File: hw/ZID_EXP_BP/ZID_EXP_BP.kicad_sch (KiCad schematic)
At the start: 41 parts, among them J1 FROM ZID, J2 Conn_02x05_2.54mm, J3 Conn_02x05_2.54mm, J4 USB-C PWR ONLY, J6 Conn_02x03_Odd_Even, J7 Conn_02x03_Odd_Even, J9 HDR 2x10 Pin, Q1 DMG2305UX, U1 74HCT138

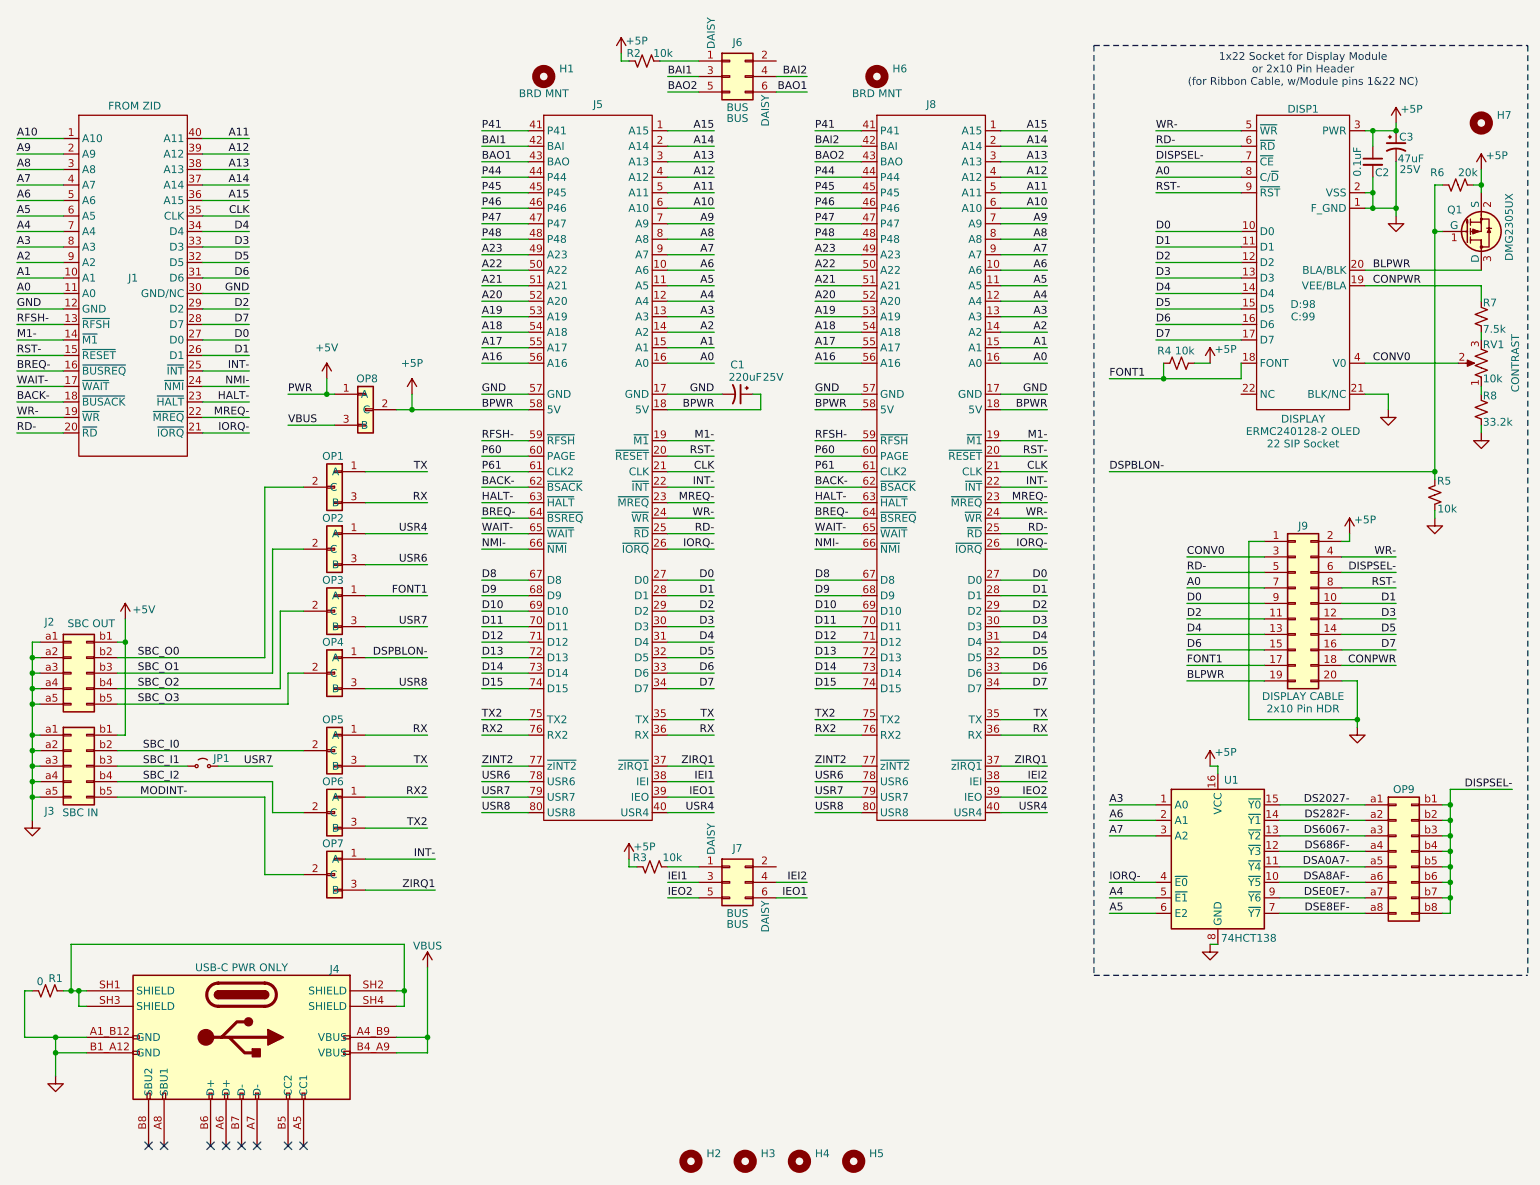
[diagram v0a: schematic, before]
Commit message: EXP-BP: Bypass caps, contrast R values
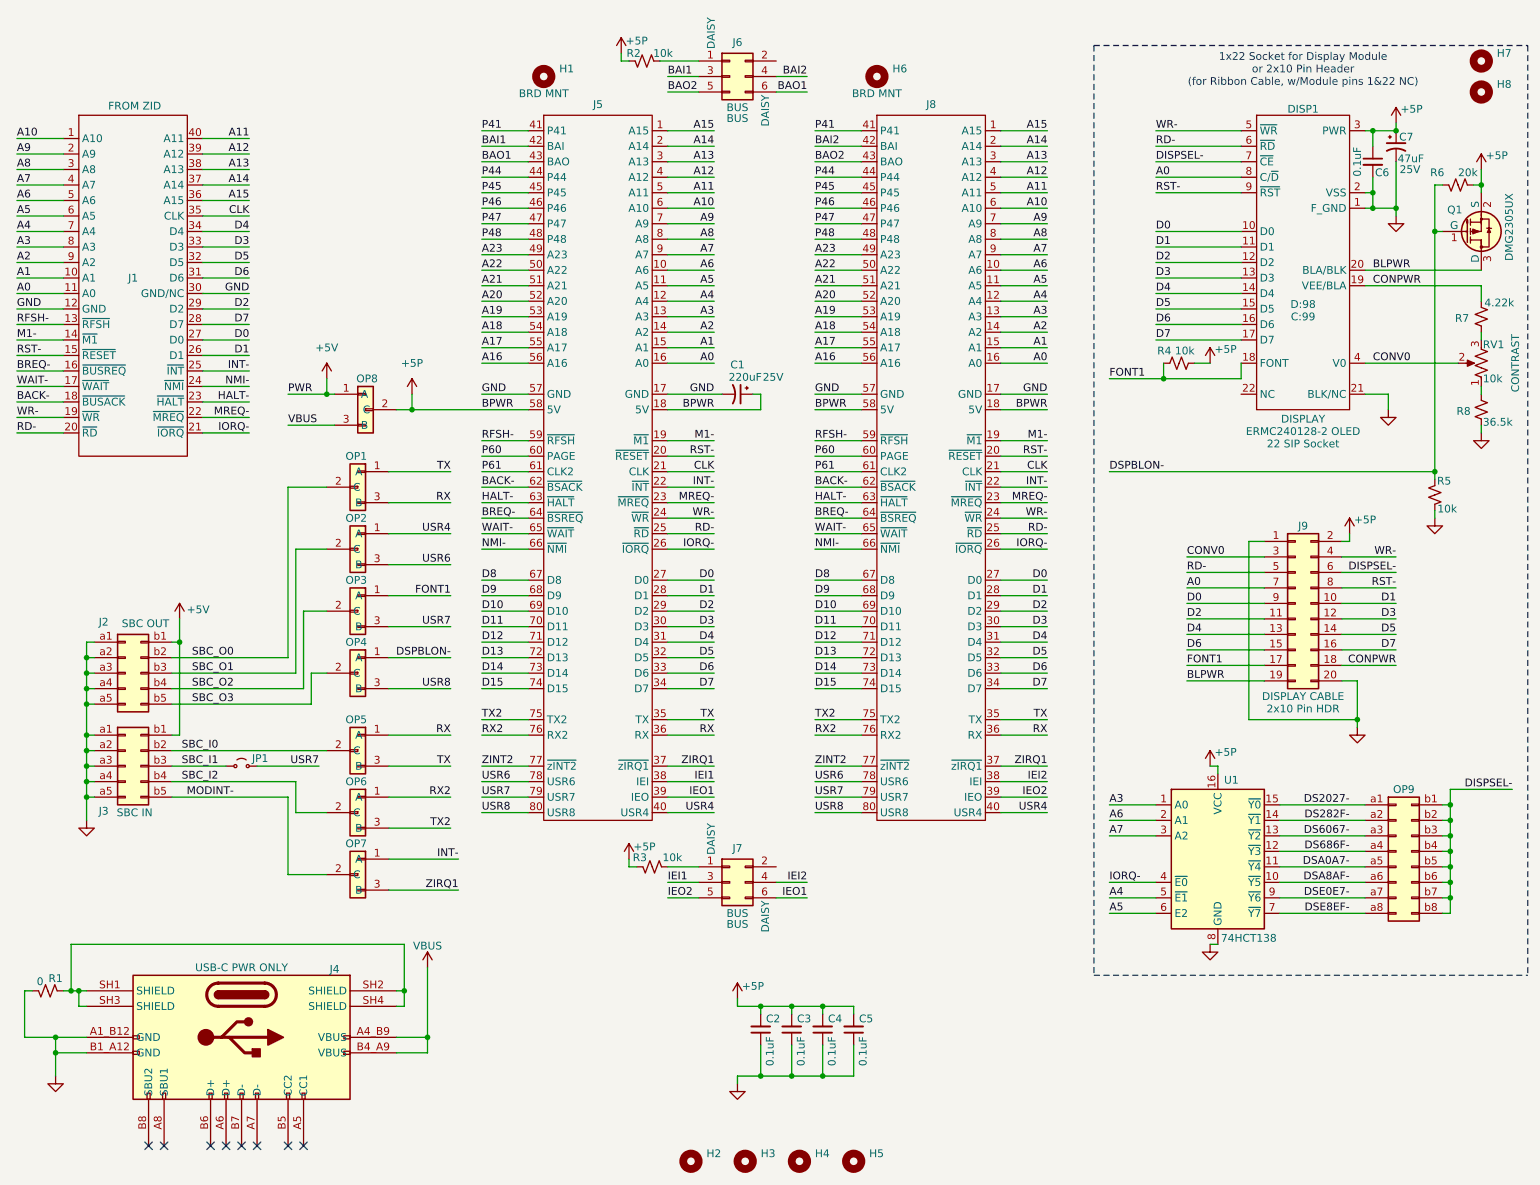
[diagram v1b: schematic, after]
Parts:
- added C2, C3, C4, C5: 0.1uF, Capacitor_SMD:C_0603_1608Metric, symbol Device:C_Small
- added H8: MountingHole, symbol Mechanical:MountingHole
- R7: value 7.5k -> 4.22k
- R8: value 33.2k -> 36.5k
- renumbered C2 to C6, C3 to C7
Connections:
- net +5P: now also C2.2, C3.2, C4.2, C5.2
- net GND: now also C2.1, C3.1, C4.1, C5.1
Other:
- moved on the sheet: H7, J2, J3, JP1, OP1, OP2, OP3, OP4, OP5, OP6, OP7

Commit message: Change ZID,POD,ExpBP connector to SIP
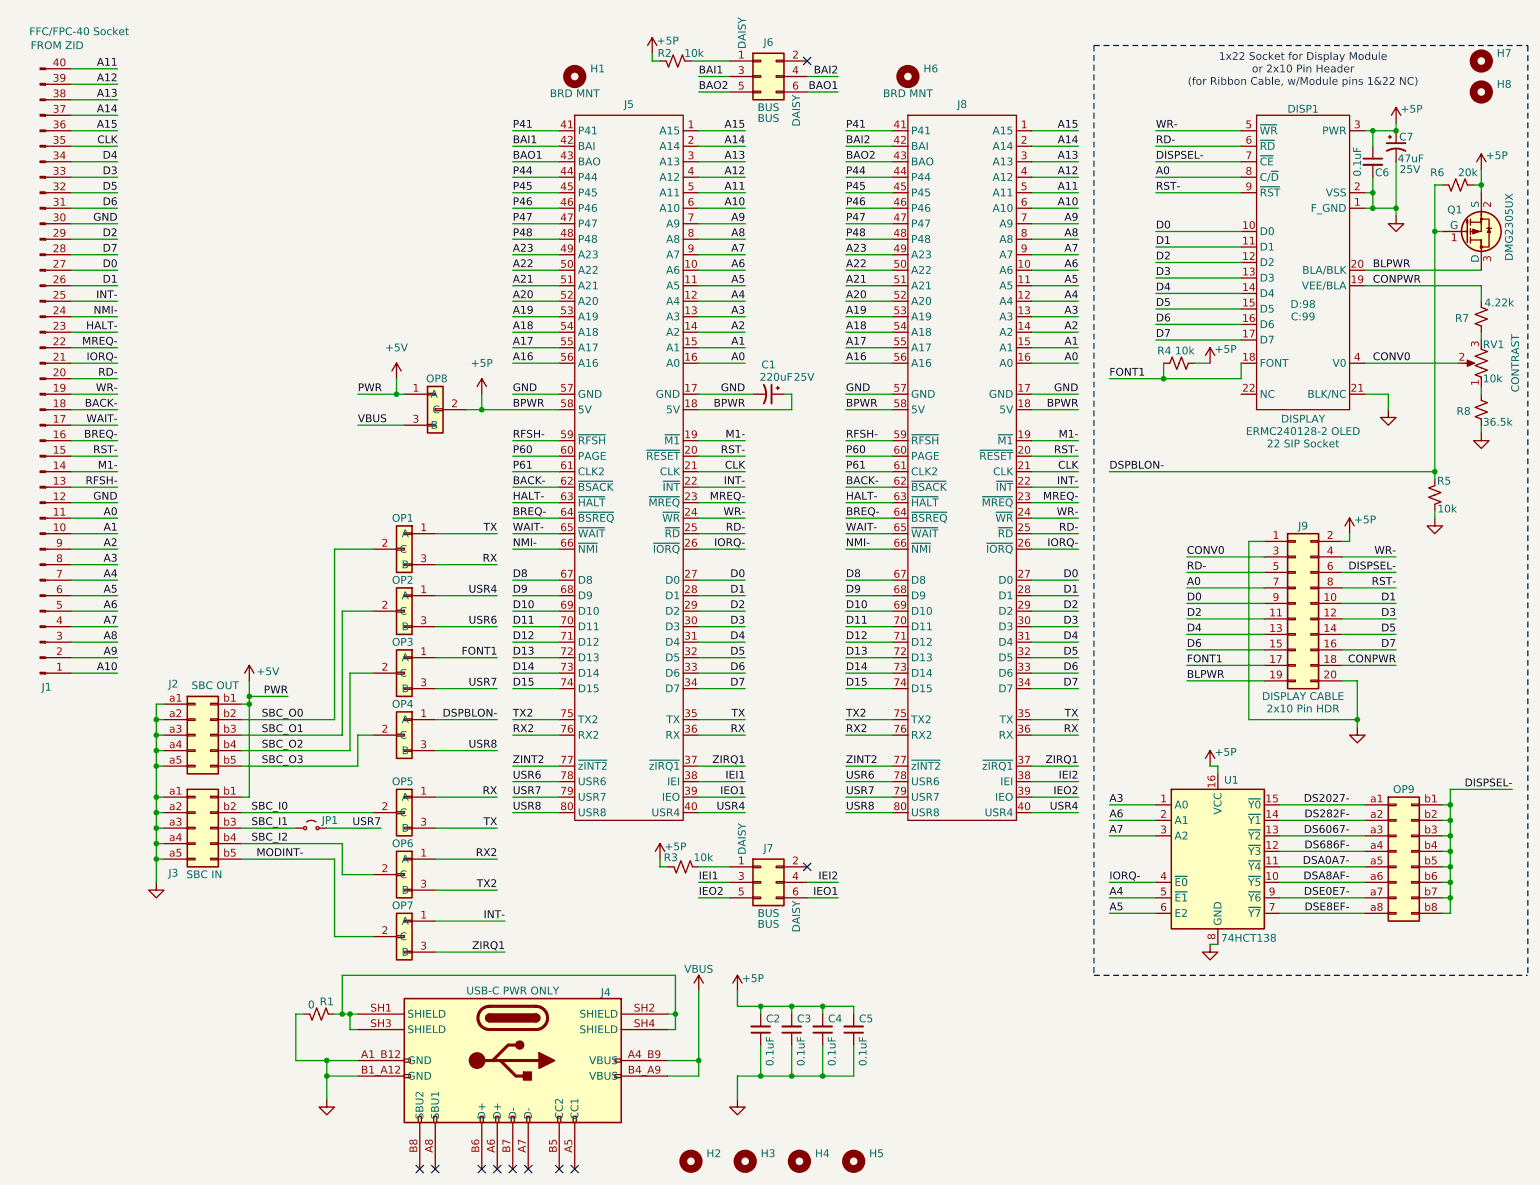
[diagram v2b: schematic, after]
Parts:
- removed J1: FROM ZID, AES_Library:CviLux_CF25401D0-05-NH_FFC-FPC-AES, symbol AES_Library:Z80-Pod-AES
- added J1: FFC/FPC-40 Socket, symbol Connector:Conn_01x40_Pin
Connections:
- net A0: now also J1.11 (Pin_11)
- net A1: now also J1.10 (Pin_10)
- net A10: now also J1.1 (Pin_1)
- net A11: now also J1.40 (Pin_40)
- net A12: now also J1.39 (Pin_39)
- net A13: now also J1.38 (Pin_38)
- net A14: now also J1.37 (Pin_37)
- net A15: now also J1.36 (Pin_36)
- net A2: now also J1.9 (Pin_9)
- net A3: now also J1.8 (Pin_8)
- net A4: now also J1.7 (Pin_7)
- net A5: now also J1.6 (Pin_6)
- net A6: now also J1.5 (Pin_5)
- net A7: now also J1.4 (Pin_4)
- net A8: now also J1.3 (Pin_3)
- net A9: now also J1.2 (Pin_2)
- net BACK-: now also J1.18 (Pin_18)
- net BREQ-: now also J1.16 (Pin_16)
- net CLK: now also J1.35 (Pin_35)
- net D0: now also J1.27 (Pin_27)
- net D1: now also J1.26 (Pin_26)
- net D2: now also J1.29 (Pin_29)
- net D3: now also J1.33 (Pin_33)
- net D4: now also J1.34 (Pin_34)
- net D5: now also J1.32 (Pin_32)
- net D6: now also J1.31 (Pin_31)
- net D7: now also J1.28 (Pin_28)
- net GND: now also J1.12 (Pin_12), J1.30 (Pin_30)
- net HALT-: now also J1.23 (Pin_23)
- net INT-: now also J1.25 (Pin_25)
- net IORQ-: now also J1.21 (Pin_21)
- net M1-: now also J1.14 (Pin_14)
- net MREQ-: now also J1.22 (Pin_22)
- net NMI-: now also J1.24 (Pin_24)
- net RD-: now also J1.20 (Pin_20)
- net RFSH-: now also J1.13 (Pin_13)
- net RST-: now also J1.15 (Pin_15)
- net WAIT-: now also J1.17 (Pin_17)
- net WR-: now also J1.19 (Pin_19)
- no-connect marks 8 -> 10
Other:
- moved on the sheet: C1, H1, H6, J2, J3, J4, J5, J6, J7, J8, JP1, OP1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

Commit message: Change bulk caps, J1 symbol
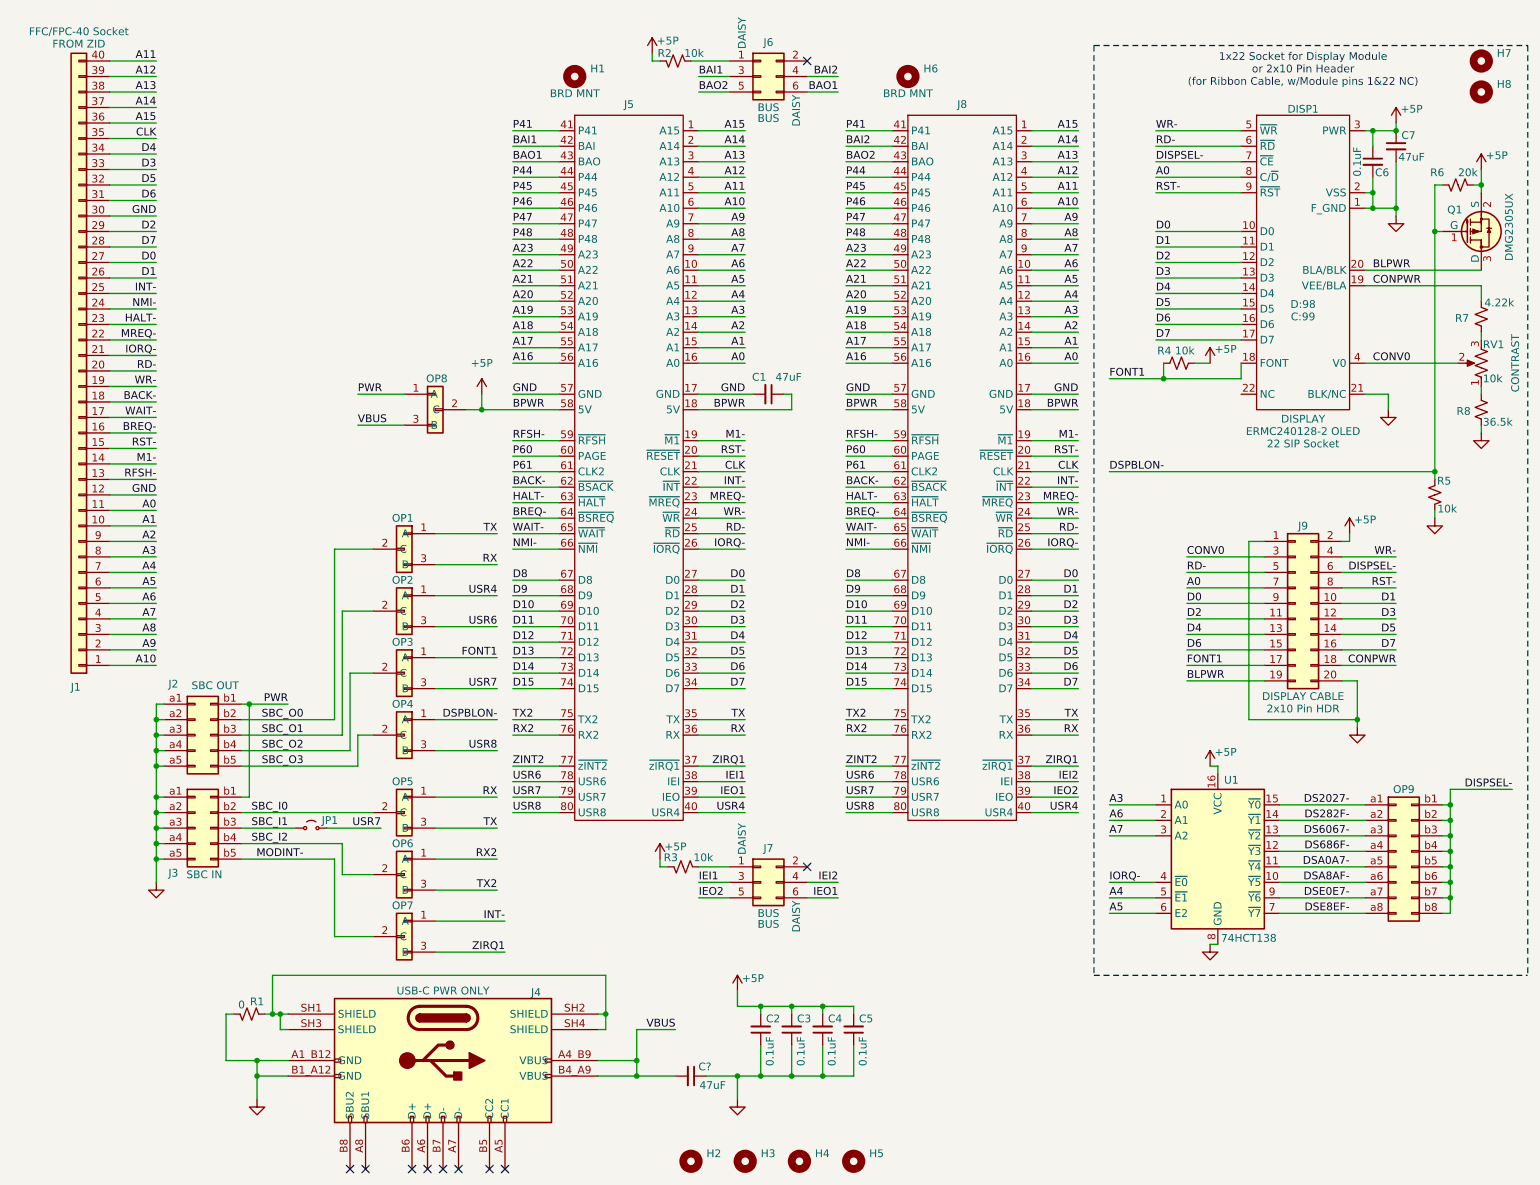
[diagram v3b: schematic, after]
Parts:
- removed C1: 220uF, Capacitor_THT:CP_Radial_D6.3mm_P2.50mm, symbol Device:C_Polarized_Small_US
- removed C7: 47uF, Capacitor_THT:CP_Radial_D4.0mm_P1.50mm, symbol Device:C_Polarized_Small_US
- removed J1: FFC/FPC-40 Socket, symbol Connector:Conn_01x40_Pin
- added C1, C7, C?: 47uF, Capacitor_SMD:C_1210_3225Metric_Pad1.33x2.70mm_HandSolder, symbol Device:C_Small
- added J1: FFC/FPC-40 Socket, symbol Connector_Generic:Conn_01x40
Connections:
- net +5P: now also C1.1, C7.1
- net A0: now also J1.11 (Pin_11)
- net A1: now also J1.10 (Pin_10)
- net A10: now also J1.1 (Pin_1)
- net A11: now also J1.40 (Pin_40)
- net A12: now also J1.39 (Pin_39)
- net A13: now also J1.38 (Pin_38)
- net A14: now also J1.37 (Pin_37)
- net A15: now also J1.36 (Pin_36)
- net A2: now also J1.9 (Pin_9)
- net A3: now also J1.8 (Pin_8)
- net A4: now also J1.7 (Pin_7)
- net A5: now also J1.6 (Pin_6)
- net A6: now also J1.5 (Pin_5)
- net A7: now also J1.4 (Pin_4)
- net A8: now also J1.3 (Pin_3)
- net A9: now also J1.2 (Pin_2)
- net BACK-: now also J1.18 (Pin_18)
- net BREQ-: now also J1.16 (Pin_16)
- net CLK: now also J1.35 (Pin_35)
- net D0: now also J1.27 (Pin_27)
- net D1: now also J1.26 (Pin_26)
- net D2: now also J1.29 (Pin_29)
- net D3: now also J1.33 (Pin_33)
- net D4: now also J1.34 (Pin_34)
- net D5: now also J1.32 (Pin_32)
- net D6: now also J1.31 (Pin_31)
- net D7: now also J1.28 (Pin_28)
- net GND: now also C1.2, C7.2, C?.1, J1.12 (Pin_12), J1.30 (Pin_30)
- net HALT-: now also J1.23 (Pin_23)
- net INT-: now also J1.25 (Pin_25)
- net IORQ-: now also J1.21 (Pin_21)
- net M1-: now also J1.14 (Pin_14)
- net MREQ-: now also J1.22 (Pin_22)
- net NMI-: now also J1.24 (Pin_24)
- net RD-: now also J1.20 (Pin_20)
- net RFSH-: now also J1.13 (Pin_13)
- net RST-: now also J1.15 (Pin_15)
- net VBUS: now also C?.2
- net WAIT-: now also J1.17 (Pin_17)
- net WR-: now also J1.19 (Pin_19)
- net +5V renamed PWR
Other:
- moved on the sheet: J4, R1
